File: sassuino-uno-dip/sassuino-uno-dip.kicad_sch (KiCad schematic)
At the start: 33 parts, among them J1 USB_B, J10 OSCPWR_HDR, J2 POWER2_HDR, J3 ICSP_HDR, J4 POWER_HDR, J5 PORTC_HDR, J6 PORTB_HDR, J7 PORTD_HDR, J8 XTAL2_HDR, J9 XTAL1_HDR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

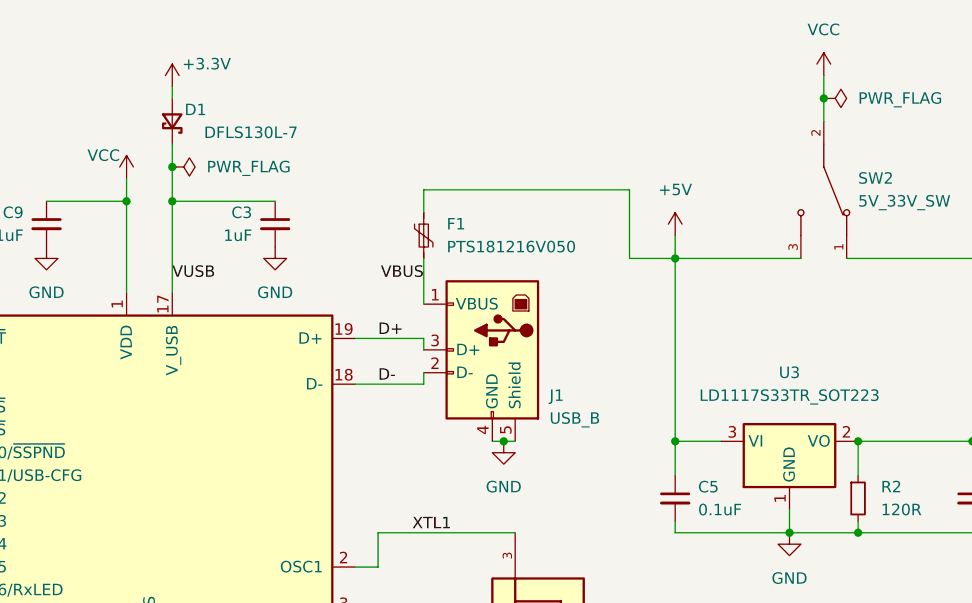
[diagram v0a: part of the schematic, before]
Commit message: Remove the diode between the two LDOs, I don't remember why it was there.
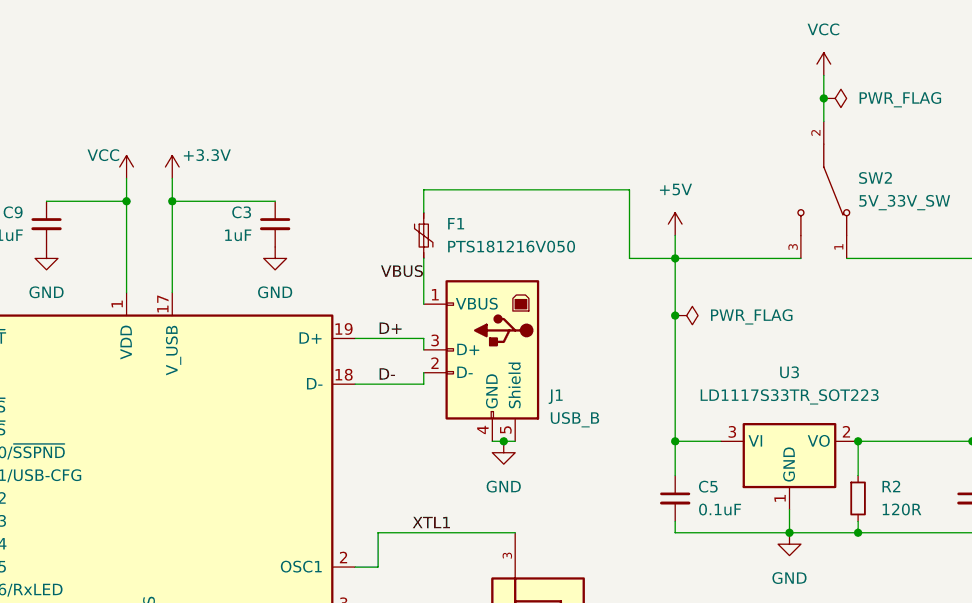
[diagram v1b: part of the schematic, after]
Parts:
- removed D1: DFLS130L-7, Diode_SMD:D_PowerDI-123, symbol Device:D_Schottky_Small
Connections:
- net VUSB is gone; now on net +3.3V: C3.1, U2.17 (V_USB)
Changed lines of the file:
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@@
 	)
 	(junction
-		(at 40.64 35.56)
+		(at 228.6 50.8)
 		(diameter 0)
 		(color 0 0 0 0)
 	)
 	(junction
-		(at 204.47 138.43)
+		(at 40.64 35.56)
 		(diameter 0)
 		(color 0 0 0 0)
 	)
 	(junction
-		(at 172.72 34.29)
+		(at 204.47 138.43)
 		(diameter 0)
 		(color 0 0 0 0)
@@
 	(wire
 		(pts
-			(xy 172.72 31.75) (xy 172.72 34.29)
+			(xy 172.72 35.56) (xy 172.72 38.1)
 		)
 		(stroke
@@
 	(wire
 		(pts
-			(xy 172.72 25.4) (xy 172.72 26.67)
-		)
-		(stroke
-			(width 0)
-			(type default)
-		)
-	)
-	(wire
-		(pts
 			(xy 58.42 106.68) (xy 60.96 106.68)
 		)
@@
 	(wire
 		(pts
-			(xy 172.72 34.29) (xy 172.72 38.1)
-		)
-		(stroke
-			(width 0)
-			(type default)
-		)
-	)
-	(wire
-		(pts
 			(xy 36.83 151.13) (xy 39.37 151.13)
 		)
@@
 	(wire
 		(pts
-			(xy 228.6 44.45) (xy 228.6 64.77)
+			(xy 228.6 44.45) (xy 228.6 50.8)
 		)
 		(stroke
@@
 	(wire
 		(pts
+			(xy 228.6 50.8) (xy 228.6 64.77)
+		)
+		(stroke
+			(width 0)
+			(type default)
+		)
+	)
+	(wire
+		(pts
 			(xy 204.47 138.43) (xy 204.47 140.97)
 		)
@@
 		)
 	)
-	(label "VUSB"
-		(at 172.72 46.99 0)
-		(effects
-			(font
-				(size 1.27 1.27)
-			)
-			(justify left bottom)
-		)
-	)
 	(label "PD6"
 		(at 132.08 172.72 180)
@@
 	)
 	(symbol
+		(lib_id "power:PWR_FLAG")
+		(at 228.6 50.8 270)
+		(unit 1)
+		(exclude_from_sim no)
+		(in_bom yes)
+		(on_board yes)
+		(dnp no)
+		(property "Reference" "#FLG01"
+			(at 230.505 50.8 0)
+			(effects
+				(font
+					(size 1.27 1.27)
+				)
+				(hide yes)
+			)
+		)
+		(property "Value" "PWR_FLAG"
+			(at 232.41 50.7999 90)
+			(effects
+				(font
+					(size 1.27 1.27)
+				)
+				(justify left)
+			)
+		)
+		(property "Footprint" ""
+			(at 228.6 50.8 0)
+			(effects
+				(font
+					(size 1.27 1.27)
+				)
+				(hide yes)
+			)
+		)
+		(property "Datasheet" "~"
+			(at 228.6 50.8 0)
+			(effects
+				(font
+					(size 1.27 1.27)
+				)
+				(hide yes)
+			)
+		)
+		(property "Description" "Special symbol for telling ERC where power comes from"
+			(at 228.6 50.8 0)
+			(effects
+				(font
+					(size 1.27 1.27)
+				)
+				(hide yes)
+			)
+		)
+		(pin "1"
+		)
+		(instances
+			(project "sassuino-uno-dip"
+				(path "/93924f32-2dd0-417f-984a-e4a0b078075b"
+					(reference "#FLG01")
+					(unit 1)
+				)
+			)
+		)
+	)
+	(symbol
 		(lib_id "power:GND")
 		(at 27.94 35.56 0)
@@
 	)
 	(symbol
-		(lib_id "power:PWR_FLAG")
-		(at 172.72 34.29 270)
-		(unit 1)
-		(exclude_from_sim no)
-		(in_bom yes)
-		(on_board yes)
-		(dnp no)
-		(fields_autoplaced yes)
-		(property "Reference" "#FLG0101"
-			(at 174.625 34.29 0)
-			(effects
-				(font
-					(size 1.27 1.27)
-				)
-				(hide yes)
-			)
-		)
-		(property "Value" "PWR_FLAG"
-			(at 176.53 34.2899 90)
-			(effects
-				(font
-					(size 1.27 1.27)
-				)
-				(justify left)
-			)
-		)
-		(property "Footprint" ""
-			(at 172.72 34.29 0)
-			(effects
-				(font
-					(size 1.27 1.27)
-				)
-				(hide yes)
-			)
-		)
-		(property "Datasheet" "~"
-			(at 172.72 34.29 0)
-			(effects
-				(font
-					(size 1.27 1.27)
-				)
-				(hide yes)
-			)
-		)
-		(property "Description" "Special symbol for telling ERC where power comes from"
-			(at 172.72 34.29 0)
-			(effects
-				(font
-					(size 1.27 1.27)
-				)
-				(hide yes)
-			)
-		)
-		(pin "1"
-		)
-		(instances
-			(project ""
-				(path "/93924f32-2dd0-417f-984a-e4a0b078075b"
-					(reference "#FLG0101")
-					(unit 1)
-				)
-			)
-		)
-	)
-	(symbol
 		(lib_id "power:VCC")
 		(at 234.95 146.05 0)
@@
 	)
 	(symbol
-		(lib_id "Device:D_Schottky_Small")
-		(at 172.72 29.21 270)
-		(mirror x)
-		(unit 1)
-		(exclude_from_sim no)
-		(in_bom yes)
-		(on_board yes)
-		(dnp no)
-		(property "Reference" "D1"
-			(at 176.53 27.94 90)
-			(effects
-				(font
-					(size 1.27 1.27)
-				)
-				(justify right)
-			)
-		)
-		(property "Value" "DFLS130L-7"
-			(at 186.69 30.48 90)
-			(effects
-				(font
-					(size 1.27 1.27)
-				)
-				(justify right)
-			)
-		)
-		(property "Footprint" "Diode_SMD:D_PowerDI-123"
-			(at 172.72 29.21 90)
-			(effects
-				(font
-					(size 1.27 1.27)
-				)
-				(hide yes)
-			)
-		)
-		(property "Datasheet" "~"
-			(at 172.72 29.21 90)
-			(effects
-				(font
-					(size 1.27 1.27)
-				)
-				(hide yes)
-			)
-		)
-		(property "Description" "Schottky diode, small symbol"
-			(at 172.72 29.21 0)
-			(effects
-				(font
-					(size 1.27 1.27)
-				)
-				(hide yes)
-			)
-		)
-		(pin "1"
-		)
-		(pin "2"
-		)
-		(instances
-			(project ""
-				(path "/93924f32-2dd0-417f-984a-e4a0b078075b"
-					(reference "D1")
-					(unit 1)
-				)
-			)
-		)
-	)
-	(symbol
 		(lib_id "Device:C_Small")
 		(at 261.62 71.12 0)
@@
 	(symbol
 		(lib_id "power:+3.3V")
-		(at 172.72 25.4 0)
+		(at 172.72 35.56 0)
 		(mirror y)
 		(unit 1)
@@
 		(dnp no)
 		(property "Reference" "#PWR02"
-			(at 172.72 29.21 0)
+			(at 172.72 39.37 0)
 			(effects
 				(font
@@
 		)
 		(property "Value" "+3.3V"
-			(at 176.53 22.86 0)
+			(at 176.53 33.02 0)
 			(effects
 				(font
@@
 		)
 		(property "Footprint" ""
-			(at 172.72 25.4 0)
+			(at 172.72 35.56 0)
 			(effects
 				(font
@@
 		)
 		(property "Datasheet" ""
-			(at 172.72 25.4 0)
+			(at 172.72 35.56 0)
 			(effects
 				(font
@@
 		)
 		(property "Description" "Power symbol creates a global label with name \"+3.3V\""
-			(at 172.72 25.4 0)
+			(at 172.72 35.56 0)
 			(effects
 				(font

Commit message: Replace crystal header 3d model with the part I'll likely be using.
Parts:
- J10, J8, J9: footprint Connector_PinSocket_2.54mm:PinSocket_1x04_P2.54mm_Vertical -> 0SassuinoFP:PinSocket_1x04_P2.54mm_Vertical_LowProfile
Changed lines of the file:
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@@
 			)
 		)
-		(property "Footprint" "Connector_PinSocket_2.54mm:PinSocket_1x04_P2.54mm_Vertical"
+		(property "Footprint" "0SassuinoFP:PinSocket_1x04_P2.54mm_Vertical_LowProfile"
 			(at 243.84 143.51 0)
 			(effects
@@
 			)
 		)
-		(property "Footprint" "Connector_PinSocket_2.54mm:PinSocket_1x04_P2.54mm_Vertical"
+		(property "Footprint" "0SassuinoFP:PinSocket_1x04_P2.54mm_Vertical_LowProfile"
 			(at 223.52 143.51 0)
 			(effects
@@
 			)
 		)
-		(property "Footprint" "Connector_PinSocket_2.54mm:PinSocket_1x04_P2.54mm_Vertical"
+		(property "Footprint" "0SassuinoFP:PinSocket_1x04_P2.54mm_Vertical_LowProfile"
 			(at 185.42 143.51 0)
 			(effects

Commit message: Various cosmetic tweaks.
Switch a few 3d models to the part I'm using.

Update the value of a few symbols to the part number.

Tweak a few traces and silkscreen bits.
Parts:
- J10: value OSCPWR_HDR -> 315-47-104-41-001000
- J8: value XTAL2_HDR -> 315-47-104-41-001000
- J9: value XTAL1_HDR -> 315-47-104-41-001000
- SW1: value RESET_SW -> 1825910-7
- SW2: value 5V_33V_SW -> SLW-883935-2A-D
- U1: footprint Package_DIP:DIP-28_W7.62mm_Socket_LongPads -> 0SassuinoFP:DIP-28_W7.62mm_Socket_LongPads
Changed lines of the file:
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@@
 			)
 		)
-		(property "Value" "RESET_SW"
+		(property "Value" "1825910-7"
 			(at 116.84 81.2799 90)
 			(effects
@@
 			)
 		)
-		(property "Description" "Push button switch, generic, symbol, four pins"
+		(property "Description" ""
 			(at 110.49 80.01 0)
 			(effects
@@
 			)
 		)
-		(property "Footprint" "Package_DIP:DIP-28_W7.62mm_Socket_LongPads"
+		(property "Footprint" "0SassuinoFP:DIP-28_W7.62mm_Socket_LongPads"
 			(at 43.18 78.74 0)
 			(effects
@@
 			)
 		)
-		(property "Description" "20MHz, 32kB Flash, 2kB SRAM, 1kB EEPROM, DIP-28"
+		(property "Description" "Socket part# ED281DT"
 			(at 43.18 78.74 0)
 			(effects
@@
 			)
 		)
-		(property "Value" "OSCPWR_HDR"
+		(property "Value" "315-47-104-41-001000"
 			(at 238.76 134.62 0)
 			(effects
@@
 			)
 		)
-		(property "Description" "Generic connector, single row, 01x04, script generated (kicad-library-utils/schlib/autogen/connector/)"
+		(property "Description" ""
 			(at 243.84 143.51 0)
 			(effects
@@
 			)
 		)
-		(property "Value" "XTAL1_HDR"
-			(at 218.44 134.62 0)
+		(property "Value" "315-47-104-41-001000"
+			(at 207.518 134.62 0)
 			(effects
 				(font
@@
 			)
 		)
-		(property "Description" "Generic connector, single row, 01x04, script generated (kicad-library-utils/schlib/autogen/connector/)"
+		(property "Description" ""
 			(at 223.52 143.51 0)
 			(effects
@@
 			)
 		)
-		(property "Value" "5V_33V_SW"
+		(property "Value" "SLW-883935-2A-D"
 			(at 248.92 38.0999 90)
 			(effects
@@
 		(on_board yes)
 		(dnp no)
-		(fields_autoplaced yes)
 		(property "Reference" "J8"
 			(at 185.42 132.08 0)
@@
 			)
 		)
-		(property "Value" "XTAL2_HDR"
-			(at 185.42 134.62 0)
+		(property "Value" "315-47-104-41-001000"
+			(at 187.452 134.62 0)
 			(effects
 				(font
@@
 			)
 		)
-		(property "Description" "Generic connector, single row, 01x04, script generated (kicad-library-utils/schlib/autogen/connector/)"
+		(property "Description" ""
 			(at 185.42 143.51 0)
 			(effects

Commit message: Add fill out part numbers in schematic
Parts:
- J1: value USB_B -> KUSBEX-BSFS1N-B
- J2: value POWER2_HDR -> PPPC041LFBN-RC
- J4: value POWER_HDR -> PPPC081LFBN-RC
- J5: value PORTC_HDR -> PPPC061LFBN-RC
- J6: value PORTB_HDR -> PPPC101LFBN-RC
- J7: value PORTD_HDR -> PPPC081LFBN-RC
- U1: value ATmega328-P -> ED3050-5-ND
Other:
- moved on the sheet: C5, C6, R2, SW2, U3

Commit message: Add a couple resistors to protect the MCP2200's TX/RX pins from the MCU.
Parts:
- added R6, R7: 1K, Resistor_SMD:R_1206_3216Metric, symbol Device:R_Small
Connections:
- net PD0/RXD: now also R6.1; no longer U2.10 (TX)
- net PD1/TXD: now also R7.1; no longer U2.12 (RX)
- new net U_RX: R7.2, U2.12 (RX)
- new net U_TX: R6.2, U2.10 (TX)
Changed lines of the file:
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@@
 	(wire
 		(pts
+			(xy 77.47 91.44) (xy 80.01 91.44)
+		)
+		(stroke
+			(width 0)
+			(type default)
+		)
+	)
+	(wire
+		(pts
 			(xy 132.08 153.67) (xy 138.43 153.67)
 		)
@@
 	(wire
 		(pts
+			(xy 77.47 93.98) (xy 80.01 93.98)
+		)
+		(stroke
+			(width 0)
+			(type default)
+		)
+	)
+	(wire
+		(pts
 			(xy 257.81 73.66) (xy 257.81 74.93)
 		)
@@
 	(wire
 		(pts
-			(xy 58.42 91.44) (xy 60.96 91.44)
+			(xy 58.42 91.44) (xy 72.39 91.44)
 		)
 		(stroke
@@
 	(wire
 		(pts
-			(xy 58.42 93.98) (xy 60.96 93.98)
+			(xy 58.42 93.98) (xy 72.39 93.98)
 		)
 		(stroke
@@
 		)
 	)
-	(label "PD1{slash}TXD"
+	(label "U_RX"
+		(at 80.01 93.98 0)
+		(effects
+			(font
+				(size 1.27 1.27)
+			)
+			(justify left bottom)
+		)
+	)
+	(label "U_RX"
 		(at 146.05 55.88 180)
 		(effects
@@
 		)
 	)
+	(label "U_TX"
+		(at 80.01 91.44 0)
+		(effects
+			(font
+				(size 1.27 1.27)
+			)
+			(justify left bottom)
+		)
+	)
 	(label "PC4{slash}SDA"
 		(at 60.96 81.28 0)
@@
 		)
 	)
-	(label "PD0{slash}RXD"
+	(label "U_TX"
 		(at 146.05 58.42 180)
 		(effects
@@
 	)
 	(symbol
+		(lib_id "Device:R_Small")
+		(at 74.93 91.44 90)
+		(unit 1)
+		(exclude_from_sim no)
+		(in_bom yes)
+		(on_board yes)
+		(dnp no)
+		(fields_autoplaced yes)
+		(property "Reference" "R6"
+			(at 74.93 86.36 90)
+			(effects
+				(font
+					(size 1.016 1.016)
+				)
+			)
+		)
+		(property "Value" "1K"
+			(at 74.93 88.9 90)
+			(effects
+				(font
+					(size 1.27 1.27)
+				)
+			)
+		)
+		(property "Footprint" "Resistor_SMD:R_1206_3216Metric"
+			(at 74.93 91.44 0)
+			(effects
+				(font
+					(size 1.27 1.27)
+				)
+				(hide yes)
+			)
+		)
+		(property "Datasheet" "~"
+			(at 74.93 91.44 0)
+			(effects
+				(font
+					(size 1.27 1.27)
+				)
+				(hide yes)
+			)
+		)
+		(property "Description" ""
+			(at 74.93 91.44 0)
+			(effects
+				(font
+					(size 1.27 1.27)
+				)
+				(hide yes)
+			)
+		)
+		(pin "2"
+		)
+		(pin "1"
+		)
+		(instances
+			(project ""
+				(path "/93924f32-2dd0-417f-984a-e4a0b078075b"
+					(reference "R6")
+					(unit 1)
+				)
+			)
+		)
+	)
+	(symbol
 		(lib_id "power:GND")
 		(at 27.94 35.56 0)
@@
 					(unit 1)
 				)
+			)
+		)
+	)
+	(symbol
+		(lib_id "Device:R_Small")
+		(at 74.93 93.98 90)
+		(unit 1)
+		(exclude_from_sim no)
+		(in_bom yes)
+		(on_board yes)
+		(dnp no)
+		(property "Reference" "R7"
+			(at 74.93 96.266 90)
+			(effects
+				(font
+					(size 1.016 1.016)
+				)
+			)
+		)
+		(property "Value" "1K"
+			(at 74.93 98.806 90)
+			(effects
+				(font
+					(size 1.27 1.27)
+				)
+			)
+		)
+		(property "Footprint" "Resistor_SMD:R_1206_3216Metric"
+			(at 74.93 93.98 0)
+			(effects
+				(font
+					(size 1.27 1.27)
+				)
+				(hide yes)
+			)
+		)
+		(property "Datasheet" "~"
+			(at 74.93 93.98 0)
+			(effects
+				(font
+					(size 1.27 1.27)
+				)
+				(hide yes)
+			)
+		)
+		(property "Description" ""
+			(at 74.93 93.98 0)
+			(effects
+				(font
+					(size 1.27 1.27)
+				)
+				(hide yes)
+			)
+		)
+		(pin "2"
+		)
+		(pin "1"
+		)
+		(instances
+			(project ""
+				(path "/93924f32-2dd0-417f-984a-e4a0b078075b"
+					(reference "R7")
+					(unit 1)
+				)
